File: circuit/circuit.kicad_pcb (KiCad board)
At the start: 2 copper layers, 31.8 x 69.8 mm, 13 parts

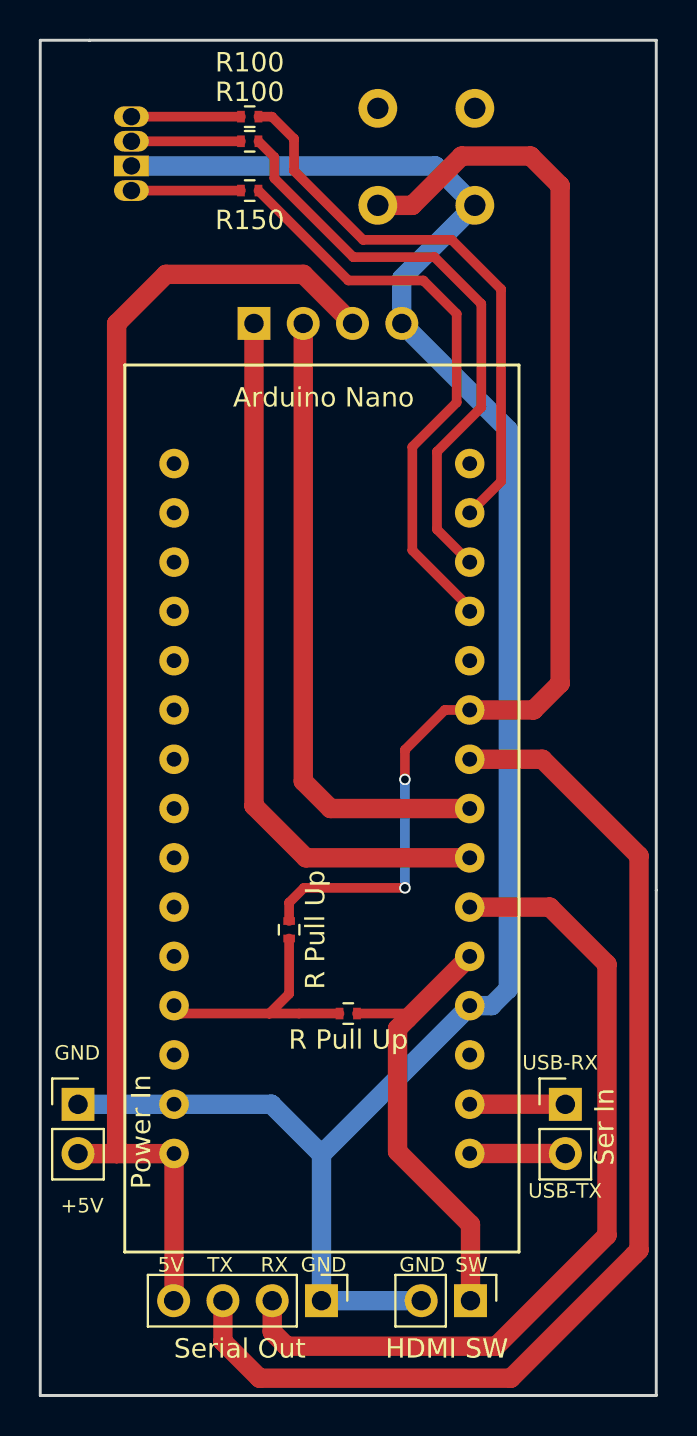
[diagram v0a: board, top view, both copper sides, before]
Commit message: Redid the I2Cwires, made Aruduino holes bigger, corrected annotations
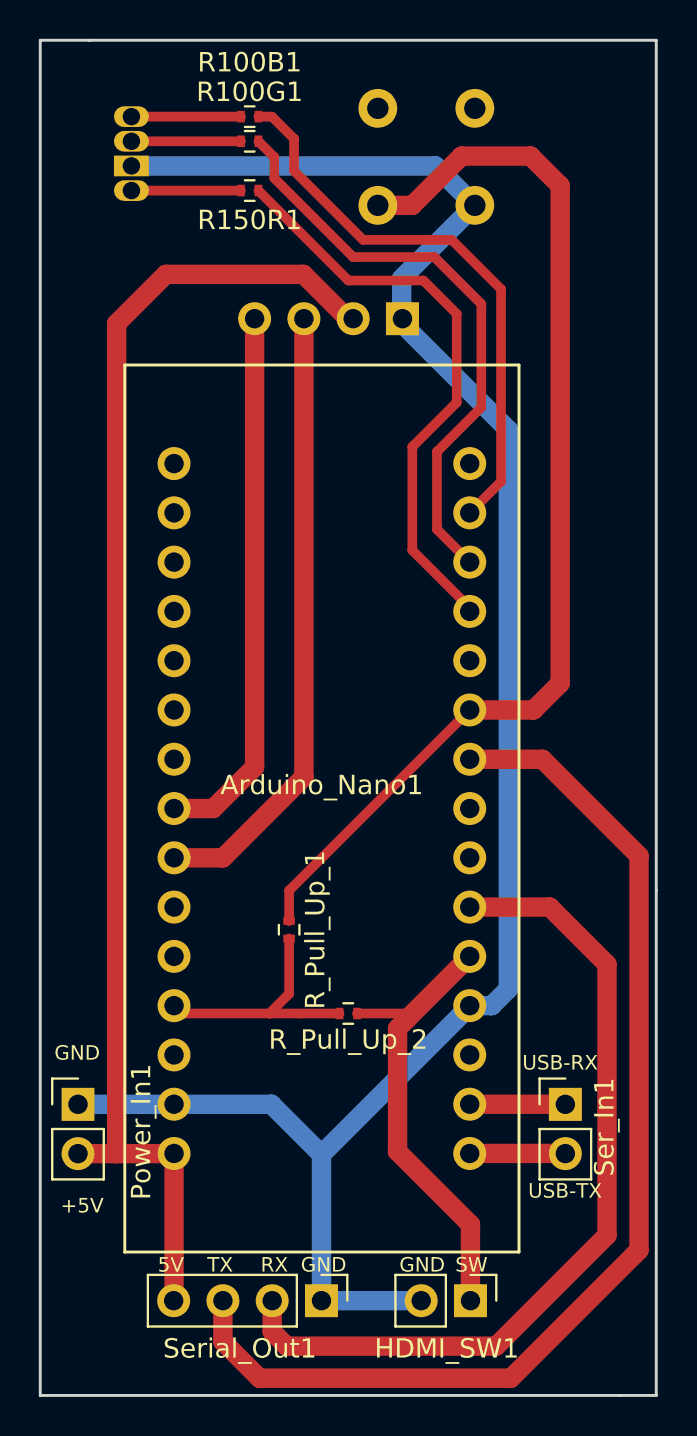
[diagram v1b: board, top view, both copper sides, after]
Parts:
- Arduino_Nano1: renamed from Arduino Nano
- HDMI_SW1: renamed from HDMI SW
- Power_In1: renamed from Power In
- Push_Button1: renamed from Push Button
- RGB_LED1: renamed from RGB LED
- R_Pull_Up_1, R_Pull_Up_2: renamed from R Pull Up
- Ser_In1: renamed from Ser In
- Serial_Out1: renamed from Serial Out
- moved OLED1 7.66 mm to (152.7, 79.8), turned to 90 degrees
- renumbered OLED to OLED1, R100 to R100B1, R100 to R100G1, R150 to R150R1
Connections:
- Arduino_Nano1 pad 3.3V: (no net) -> Net-(Arduino_Nano1-Pad3.3V)
- Arduino_Nano1 pad A0: (no net) -> Net-(Arduino_Nano1-PadA0)
- Arduino_Nano1 pad A1: (no net) -> Net-(Arduino_Nano1-PadA1)
- Arduino_Nano1 pad A2: (no net) -> Net-(Arduino_Nano1-PadA2)
- Arduino_Nano1 pad A3: (no net) -> Net-(Arduino_Nano1-PadA3)
- Arduino_Nano1 pad A4: (no net) -> Net-(Arduino_Nano1-PadA4)
- Arduino_Nano1 pad A5: (no net) -> Net-(Arduino_Nano1-PadA5)
- Arduino_Nano1 pad A6: (no net) -> Net-(Arduino_Nano1-PadA6)
- Arduino_Nano1 pad A7: (no net) -> Net-(Arduino_Nano1-PadA7)
- Arduino_Nano1 pad D12: (no net) -> Net-(Arduino_Nano1-PadD12)
- Arduino_Nano1 pad D13: (no net) -> Net-(Arduino_Nano1-PadD13)
- Arduino_Nano1 pad D4: Net-(J6-Pad1) -> Net-(Arduino_Nano1-PadD4)
- Arduino_Nano1 pad D5: Net-(J6-Pad2) -> Net-(Arduino_Nano1-PadD5)
- Arduino_Nano1 pad D8: (no net) -> Net-(Arduino_Nano1-PadD8)
- Arduino_Nano1 pad REF: (no net) -> Net-(Arduino_Nano1-PadREF)
- OLED1 pad 1: Net-(J6-Pad1) -> GND
- OLED1 pad 2: Net-(J6-Pad2) -> +5V
- OLED1 pad 3: +5V -> Net-(Arduino_Nano1-PadA5)
- OLED1 pad 4: GND -> Net-(Arduino_Nano1-PadA4)
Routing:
- net Net-(J6-Pad1): track 37.1 -> 0.00 mm
- net Net-(J6-Pad2): track 32.8 -> 0.00 mm
- net Net-(Arduino_Nano1-PadA5): track 0.00 -> 32.0 mm
- net Net-(Arduino_Nano1-PadA4): track 0.00 -> 28.2 mm
- net Net-(Arduino_Nano1-PadD7): track 60.5 -> 56.7 mm, vias 2 -> 0
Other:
- board text added: "Box Display - v0.2 Connects an OLED diplay, switch, and a RGB LED for box feedback. Provides for manual control of HDMI matrix. - LeStarch & Pelmini- 2018"
- board text removed: "Box Display - v0.1 Connects an OLED diplay, switch, and a RGB LED for box feedback. Provides for manual control of HDMI matrix. - LeStarch - 2018"
